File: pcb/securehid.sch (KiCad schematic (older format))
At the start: 93 parts

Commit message: Initial PCB draft
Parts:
- removed C?: 100n, symbol device:C_Small
- removed D? (x4): Ice blue, symbol device:LED
- removed D?: ice blue, symbol device:LED
- removed D? (x5): pink, symbol device:LED
- added C13, C16, C19, C22: 12p, Capacitor_SMD:C_0603_1608Metric_Pad1.05x0.95mm_HandSolder, symbol device:C_Small
- added C30, C31, C35, C36: 100n, Capacitor_SMD:C_0603_1608Metric_Pad1.05x0.95mm_HandSolder, symbol device:C_Small
- added C32, C33: 100n, Capacitor_SMD:C_0603_1608Metric_Pad1.05x0.95mm_HandSolder, symbol device:C
- added C34: 47u, Capacitor_SMD:C_Elec_6.3x5.8, symbol device:CP
- added D11, D12, D13, D14, D15: pink, LED_SMD:LED_PLCC_2835_Handsoldering, symbol device:LED
- added D5, D6, D7, D8, D9: Ice blue, LED_SMD:LED_PLCC_2835_Handsoldering, symbol device:LED
- added J4: SWD_DEVICE, Connector_PinHeader_2.54mm:PinHeader_1x04_P2.54mm_Vertical, symbol Connector_Generic:Conn_01x04
- added R2, R3: 10k, Resistor_SMD:R_0603_1608Metric_Pad1.05x0.95mm_HandSolder, symbol device:R_Small
- added R26: NETTIE, NetTie:NetTie-2_SMD_Pad2.0mm, symbol device:R_Small
- added R4: 1M, Resistor_SMD:R_0603_1608Metric_Pad1.05x0.95mm_HandSolder, symbol device:R_Small
- added TP1, TP10, TP11, TP12, TP13, TP14, TP15, TP16, TP17, TP18, TP19, TP2, TP20, TP21, TP22, TP23, TP24, TP25, TP26, TP27, TP28, TP29, TP3, TP30, TP31, TP32, TP33, TP34, TP35, TP36, TP37, TP38, TP39, TP4, TP40, TP41, TP42, TP43, TP44, TP45, TP46, TP47, TP48, TP49, TP5, TP50, TP51, TP52, TP53, TP54, TP55, TP56, TP57, TP58, TP59, TP6, TP60, TP61, TP62, TP63, TP64, TP65, TP66, TP67, TP68, TP69, TP7, TP70, TP71, TP72, TP73, TP74, TP75, TP76, TP77, TP78, TP79, TP8, TP80, TP9: TestPoint_Alt, TestPoint:TestPoint_Pad_1.0x1.0mm, symbol Connector:TestPoint_Alt
- added U5: AP1117-33, TO_SOT_Packages_SMD:SOT-223-3Lead_TabPin2, symbol regul:AP1117-33
- added Y1: 8MHz, Crystal:Crystal_SMD_TXC_7M-4Pin_3.2x2.5mm, symbol device:Crystal_GND24_Small
- added Y3: 32.768kHz, Crystal:Crystal_SMD_TXC_7M-4Pin_3.2x2.5mm, symbol device:Crystal_GND24_Small
- BT1: renamed from BT?; footprint (none) -> Battery:BatteryHolder_MPD_BC2003_1x2032
- C1, C10, C11, C14, C15, C17, C18, C2, C20, C21, C23, C24, C26, C28, C29, C4, C5, C6, C7, C8: renamed from C?; footprint (none) -> Capacitor_SMD:C_0603_1608Metric_Pad1.05x0.95mm_HandSolder
- C12, C25, C27: renamed from C?; footprint (none) -> Capacitor_SMD:C_Elec_6.3x5.8; ali (none) -> https://www.aliexpress.com/item//32846711940.html
- C9: renamed from C?; footprint (none) -> Capacitor_SMD:C_Elec_10x10.2; ali (none) -> https://www.aliexpress.com/item//32556865449.html
- D1, D16, D17, D18, D19, D2, D20, D21, D22, D23, D24, D3: renamed from D?; footprint (none) -> LED_SMD:LED_0603_1608Metric_Pad1.05x0.95mm_HandSolder
- D10: renamed from D?; footprint (none) -> LED_SMD:LED_PLCC_2835_Handsoldering; ali (none) -> https://www.aliexpress.com/item//32376752790.html
- D4: renamed from D?; footprint (none) -> LED_SMD:LED_PLCC_2835_Handsoldering; ali (none) -> https://www.aliexpress.com/store/product//1758868_326936840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
- J1: renamed from J?; footprint (none) -> Connector_USB:USB_Micro-B_GCT_USB3076-30-A
- J2: renamed from J?; value SWD -> SWD_HOST; footprint (none) -> Connector_PinHeader_2.54mm:PinHeader_1x04_P2.54mm_Vertical
- J3, J5: renamed from J?; footprint (none) -> Connector_PinHeader_2.54mm:PinHeader_1x04_P2.54mm_Vertical
- J6, J8: renamed from J?; footprint (none) -> footprints:USB_A_FEMALE_THT; ali (none) -> https://www.aliexpress.com/item//32849715796.html
- J7: renamed from J?; footprint (none) -> Connector_PinHeader_2.54mm:PinHeader_2x05_P2.54mm_Vertical
- LS1: renamed from LS?; footprint (none) -> Buzzer_Beeper:Buzzer_12x9.5RM7.6; ali (none) -> https://www.aliexpress.com/item//32503620431.html
- R1, R10, R11, R12, R13, R14, R15, R16, R17, R18, R19, R20, R21, R22, R23, R24, R25, R5, R6, R7, R8, R9: renamed from R?; footprint (none) -> Resistor_SMD:R_0603_1608Metric_Pad1.05x0.95mm_HandSolder
- RN1, RN2, RN3: renamed from RN?; footprint (none) -> Resistor_SMD:R_Array_Convex_4x0603; marutsu (none) -> https://www.marutsu.co.jp/pc/i/14222/
- SW1: renamed from SW?; footprint (none) -> Button_Switch_SMD:SW_SPST_EVPBF
- U2: renamed from U?; value STM32F103C8Tx -> STM32F103C8T6
- U3: renamed from U?; value STM32F407VETx -> STM32F407VET6
- U4: renamed from U?; footprint (none) -> Package_SO:SSOP-28_3.9x9.9mm_P0.635mm; ali (none) -> https://www.aliexpress.com/item//32787809220.html
- Y2, Y4: renamed from Y?; footprint (none) -> Crystal:Crystal_SMD_TXC_7M-4Pin_3.2x2.5mm
- gave numbers to parts that had none: 4
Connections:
- net +3V3: now also J4.1 (Pin_1), R2.2; no longer R6.1
- net DBGD_RX: now also U2.31 (PA10)
- net DBGD_TX: now also U2.30 (PA9)
- net GND: now also U3.94 (BOOT0), Y4.2, Y4.4, C19.1, C22.1, C30.1, R26.1, Y3.2, Y3.4; no longer J2.3 (Pin_3), J3.2 (Pin_2), J5.2 (Pin_2)
- net HUB_NRST: now also C30.2
- net LED0: now also RN1.8 (R1.2); no longer D1.1 (K)
- net LED1: now also RN1.7 (R2.2); no longer D2.1 (K)
- net LED10: now also RN3.6 (R3.2); no longer D23.1 (K)
- net LED11: now also RN3.5 (R4.2); no longer D24.1 (K)
- net LED2: now also RN1.6 (R3.2); no longer D3.1 (K)
- net LED3: now also RN1.5 (R4.2); no longer D16.1 (K)
- net LED4: now also RN2.8 (R1.2); no longer D17.1 (K)
- net LED5: now also RN2.7 (R2.2); no longer D18.1 (K)
- net LED6: now also RN2.6 (R3.2); no longer D19.1 (K)
- net LED7: now also RN2.5 (R4.2); no longer D20.1 (K)
- net LED8: now also RN3.8 (R1.2); no longer D21.1 (K)
- net LED9: now also RN3.7 (R2.2); no longer D22.1 (K)
- net SECURE_IF_F4RX: now also U2.12 (PA2)
- net SECURE_IF_F4TX: now also U2.13 (PA3)
- net USBD_DM: now also U2.32 (PA11)
- net USBD_DP: now also U2.33 (PA12)
- net VBUS: now also D1.2 (A), D10.2 (A), D16.2 (A), D17.2 (A), D18.2 (A), D19.2 (A), D2.2 (A), D20.2 (A), D21.2 (A), D22.2 (A), D23.2 (A), D24.2 (A), D3.2 (A), D4.2 (A), C32.1, D11.2 (A), D12.2 (A), D13.2 (A), D14.2 (A), D15.2 (A), D5.2 (A), D6.2 (A), D7.2 (A), D8.2 (A), D9.2 (A), U5.3 (VI); no longer R12.1, R13.1, R14.1, R15.1, R16.1, R17.1, R18.1, R19.1, R20.1, R21.1, R22.1, R23.1, RN1.1 (R1.1), RN1.2 (R2.1), RN1.3 (R3.1), RN1.4 (R4.1), RN2.1 (R1.1), RN2.2 (R2.1), RN2.3 (R3.1), RN2.4 (R4.1), RN3.1 (R1.1), RN3.2 (R2.1), RN3.3 (R3.1), RN3.4 (R4.1)
- net at U3.1 (PE2): now also TP27.1
- net at U3.14 (NRST): now also R2.1
- net at U3.15 (PC0): now also TP52.1
- net at U3.16 (PC1): now also TP54.1
- net at U3.17 (PC2): now also TP56.1
- net at U3.18 (PC3): now also TP58.1
- net at U3.23 (PA0): now also TP1.1
- net at U3.24 (PA1): now also TP2.1
- net at U3.29 (PA4): now also TP3.1
- net at U3.33 (PC4): now also TP60.1
- net at U3.34 (PC5): now also TP62.1
- net at U3.35 (PB0): now also TP20.1
- net at U3.36 (PB1): now also TP24.1
- net at U3.37 (PB2): now also TP28.1
- net at U3.48 (PB11): now also TP46.1
- net at U3.51 (PB12): now also TP47.1
- net at U3.52 (PB13): now also TP48.1
- net at U3.53 (PB14): now also TP49.1
- net at U3.54 (PB15): now also TP50.1
- net at U3.55 (PD8): now also TP67.1
- net at U3.56 (PD9): now also TP69.1
- net at U3.57 (PD10): now also TP71.1
- net at U3.58 (PD11): now also TP73.1
- net at U3.59 (PD12): now also TP75.1
- net at U3.60 (PD13): now also TP77.1
- net at U3.61 (PD14): now also TP79.1
- net at U3.62 (PD15): now also TP80.1
- net at U3.63 (PC6): now also TP64.1
- net at U3.64 (PC7): now also TP66.1
- net at U3.65 (PC8): now also TP68.1
- net at U3.66 (PC9): now also TP70.1
- net at U3.67 (PA8): now also TP5.1
- net at U3.7 (PC13): now also TP78.1
- net at U3.77 (PA15): now also TP14.1
- net at U3.78 (PC10): now also TP72.1
- net at U3.79 (PC11): now also TP74.1
- net at U3.8 (PC14): now also C19.2, Y3.1
- net at U3.80 (PC12): now also TP76.1
- net at U3.81 (PD0): now also TP51.1
- net at U3.82 (PD1): now also TP53.1
- net at U3.83 (PD2): now also TP55.1
- net at U3.84 (PD3): now also TP57.1
- net at U3.85 (PD4): now also TP59.1
- net at U3.86 (PD5): now also TP61.1
- net at U3.87 (PD6): now also TP63.1
- net at U3.88 (PD7): now also TP65.1
- net at U3.89 (PB3): now also TP31.1
- net at U3.9 (PC15): now also C22.2, Y3.3
- net at U3.90 (PB4): now also TP33.1
- net at U3.91 (PB5): now also TP35.1
- net at U3.92 (PB6): now also TP37.1
- net at U3.93 (PB7): now also TP39.1
- net at U3.95 (PB8): now also TP41.1
- net at U3.96 (PB9): now also TP43.1
- net at U3.97 (PE0): now also TP19.1
- net at U3.98 (PE1): now also TP23.1
- net +3.3VA: now reaches U2.1 (VBAT)
- net +3.3VA: now also R6.1, U2.24 (VDD), U2.36 (VDD), U2.48 (VDD), U2.9 (VDDA), C31.1, C33.1, C34.1, C35.1, C36.1, R3.1, U5.2 (VO)
- net at U2.10 (PA0): now also TP9.1
- net at U2.11 (PA1): now also TP11.1
- net at U2.14 (PA4): now also TP16.1
- net at U2.15 (PA5): now also TP18.1
- net at U2.16 (PA6): now also TP22.1
- net at U2.17 (PA7): now also TP26.1
- net at U2.18 (PB0): now also TP8.1
- net at U2.19 (PB1): now also TP10.1
- net at U2.2 (PC13): now also TP4.1
- net at U2.20 (PB2): now also TP12.1
- net at U2.21 (PB10): now also TP34.1
- net at U2.22 (PB11): now also TP36.1
- net GNDA: now reaches U2.23 (VSS)
- net GNDA: now also J2.3 (Pin_3), J3.2 (Pin_2), J5.2 (Pin_2), U2.35 (VSS), U2.44 (BOOT0), U2.47 (VSS), U2.8 (VSSA), C13.1, C16.1, C31.2, C32.2, C33.2, C34.2, C35.2, C36.2, J4.3 (Pin_3), R26.2, U5.1 (GND), Y1.2, Y1.4
- net at U2.25 (PB12): now also TP38.1
- net at U2.26 (PB13): now also TP40.1
- net at U2.27 (PB14): now also TP42.1
- net at U2.28 (PB15): now also TP44.1
- net at U2.29 (PA8): now also TP30.1
- net at U2.3 (PC14): now also TP6.1
- net SWDIOD: now reaches U2.34 (PA13)
- net SWDIOD: now also J4.4 (Pin_4)
- net SWCLKD: now reaches U2.37 (PA14)
- net SWCLKD: now also J4.2 (Pin_2)
- net at U2.38 (PA15): now also TP45.1
- net at U2.39 (PB3): now also TP13.1
- net at U2.4 (PC15): now also TP7.1
- net at U2.40 (PB4): now also TP15.1
- net at U2.41 (PB5): now also TP17.1
- net at U2.42 (PB6): now also TP21.1
- net at U2.43 (PB7): now also TP25.1
- net at U2.45 (PB8): now also TP29.1
- net at U2.46 (PB9): now also TP32.1
- net at U2.5 (PD0): now also C13.2, R4.1, Y1.1
- net at U2.6 (PD1): now also C16.2, R4.2, Y1.3
- net at U2.7 (NRST): now also R3.2
- net at Q1.2 (S): now also R12.2, R13.2, R14.2, R15.2, R16.2, R17.2; no longer D4.1 (K)
- net at Q2.2 (S): now also R18.2, R19.2, R20.2, R21.2, R22.2, R23.2; no longer D10.1 (K)
- net SWCLK renamed SWCLKH
- net SWDIO renamed SWDIOH
- new net: D4.1 (K), R12.1
- new net: D5.1 (K), R13.1
- new net: D6.1 (K), R14.1
- new net: D7.1 (K), R15.1
- new net: D8.1 (K), R16.1
- new net: D9.1 (K), R17.1
- new net: D10.1 (K), R18.1
- new net: D11.1 (K), R19.1
- new net: D12.1 (K), R20.1
- new net: D13.1 (K), R21.1
- new net: D14.1 (K), R22.1
- new net: D15.1 (K), R23.1
- new net: D1.1 (K), RN1.1 (R1.1)
- new net: D2.1 (K), RN1.2 (R2.1)
- new net: D3.1 (K), RN1.3 (R3.1)
- new net: D16.1 (K), RN1.4 (R4.1)
- new net: D17.1 (K), RN2.1 (R1.1)
- new net: D18.1 (K), RN2.2 (R2.1)
- new net: D19.1 (K), RN2.3 (R3.1)
- new net: D20.1 (K), RN2.4 (R4.1)
- new net: D21.1 (K), RN3.1 (R1.1)
- new net: D22.1 (K), RN3.2 (R2.1)
- new net: D23.1 (K), RN3.3 (R3.1)
- new net: D24.1 (K), RN3.4 (R4.1)
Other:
- moved on the sheet: C10, C11, C12, C9, D10, D4, J1, J2, J3, J5, R12, R13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

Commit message: Some cleanups
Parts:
- added TP81, TP82, TP?: TestPoint_Alt, TestPoint:TestPoint_Pad_1.0x1.0mm, symbol Connector:TestPoint_Alt
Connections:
- net GNDA: now also TP?.1
- net SECURE_IF_F4RX: now also TP81.1
- net SECURE_IF_F4TX: now also TP82.1
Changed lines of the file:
@@
 Wire Wire Line
 	13450 4250 14150 4250
-Text Label 14150 3550 2    50   ~ 0
+Text Label 15100 3550 2    50   ~ 0
 SECURE_IF_F4RX
-Text Label 14150 3650 2    50   ~ 0
+Text Label 15100 3650 2    50   ~ 0
 SECURE_IF_F4TX
-Wire Wire Line
-	14150 3650 13450 3650
-Wire Wire Line
-	13450 3550 14150 3550
 $Comp
 L device:Crystal_GND24_Small Y3
@@
 Wire Wire Line
 	1950 1250 2750 1250
+$Comp
+L Connector:TestPoint_Alt TP81
+U 1 1 5BFF0539
+P 14400 3500
+F 0 "TP81" V 14400 3800 50  0000 C CNN
+F 1 "TestPoint_Alt" V 14504 3574 50  0001 C CNN
+F 2 "TestPoint:TestPoint_Pad_1.0x1.0mm" H 14600 3500 50  0001 C CNN
+F 3 "~" H 14600 3500 50  0001 C CNN
+	1    14400 3500
+	0    -1   -1   0
+$EndComp
+$Comp
+L Connector:TestPoint_Alt TP82
+U 1 1 5C0015E1
+P 14400 3600
+F 0 "TP82" V 14400 3900 50  0000 C CNN
+F 1 "TestPoint_Alt" V 14504 3674 50  0001 C CNN
+F 2 "TestPoint:TestPoint_Pad_1.0x1.0mm" H 14600 3600 50  0001 C CNN
+F 3 "~" H 14600 3600 50  0001 C CNN
+	1    14400 3600
+	0    -1   -1   0
+$EndComp
+Wire Wire Line
+	13450 3650 14400 3650
+Wire Wire Line
+	13450 3550 14400 3550
+Wire Wire Line
+	14400 3500 14400 3550
+Connection ~ 14400 3550
+Wire Wire Line
+	14400 3550 15100 3550
+Wire Wire Line
+	14400 3600 14400 3650
+Connection ~ 14400 3650
+Wire Wire Line
+	14400 3650 15100 3650
+$Comp
+L Connector:TestPoint_Alt TP?
+U 1 1 5C13B94B
+P 14400 3700
+F 0 "TP?" V 14400 4000 50  0000 C CNN
+F 1 "TestPoint_Alt" V 14504 3774 50  0001 C CNN
+F 2 "TestPoint:TestPoint_Pad_1.0x1.0mm" H 14600 3700 50  0001 C CNN
+F 3 "~" H 14600 3700 50  0001 C CNN
+	1    14400 3700
+	0    -1   -1   0
+$EndComp
+$Comp
+L power:GNDA #PWR?
+U 1 1 5C14109B
+P 14400 3700
+F 0 "#PWR?" H 14400 3450 50  0001 C CNN
+F 1 "GNDA" H 14405 3527 50  0000 C CNN
+F 2 "" H 14400 3700 50  0001 C CNN
+F 3 "" H 14400 3700 50  0001 C CNN
+	1    14400 3700
+	1    0    0    -1
+$EndComp
 $EndSCHEMATC

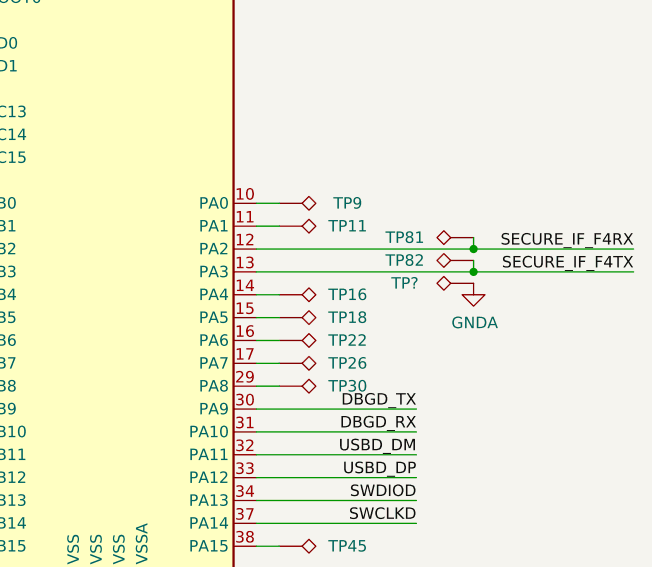
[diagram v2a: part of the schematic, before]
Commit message: Further PCB cleanup, initial silk cleanup
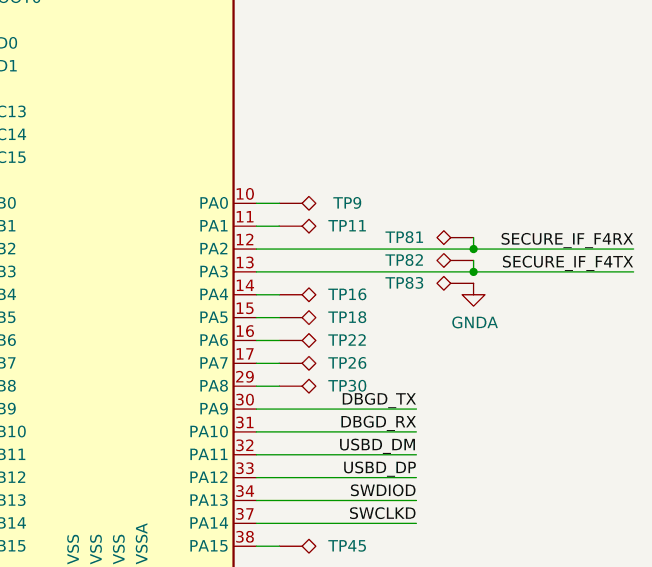
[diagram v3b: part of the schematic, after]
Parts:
- gave numbers to parts that had none: 1
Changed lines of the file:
@@
 	14400 3650 15100 3650
 $Comp
-L Connector:TestPoint_Alt TP?
+L Connector:TestPoint_Alt TP83
 U 1 1 5C13B94B
 P 14400 3700
-F 0 "TP?" V 14400 4000 50  0000 C CNN
+F 0 "TP83" V 14400 4000 50  0000 C CNN
 F 1 "TestPoint_Alt" V 14504 3774 50  0001 C CNN
 F 2 "TestPoint:TestPoint_Pad_1.0x1.0mm" H 14600 3700 50  0001 C CNN
@@
 $EndComp
 $Comp
-L power:GNDA #PWR?
+L power:GNDA #PWR0160
 U 1 1 5C14109B
 P 14400 3700
-F 0 "#PWR?" H 14400 3450 50  0001 C CNN
+F 0 "#PWR0160" H 14400 3450 50  0001 C CNN
 F 1 "GNDA" H 14405 3527 50  0000 C CNN
 F 2 "" H 14400 3700 50  0001 C CNN

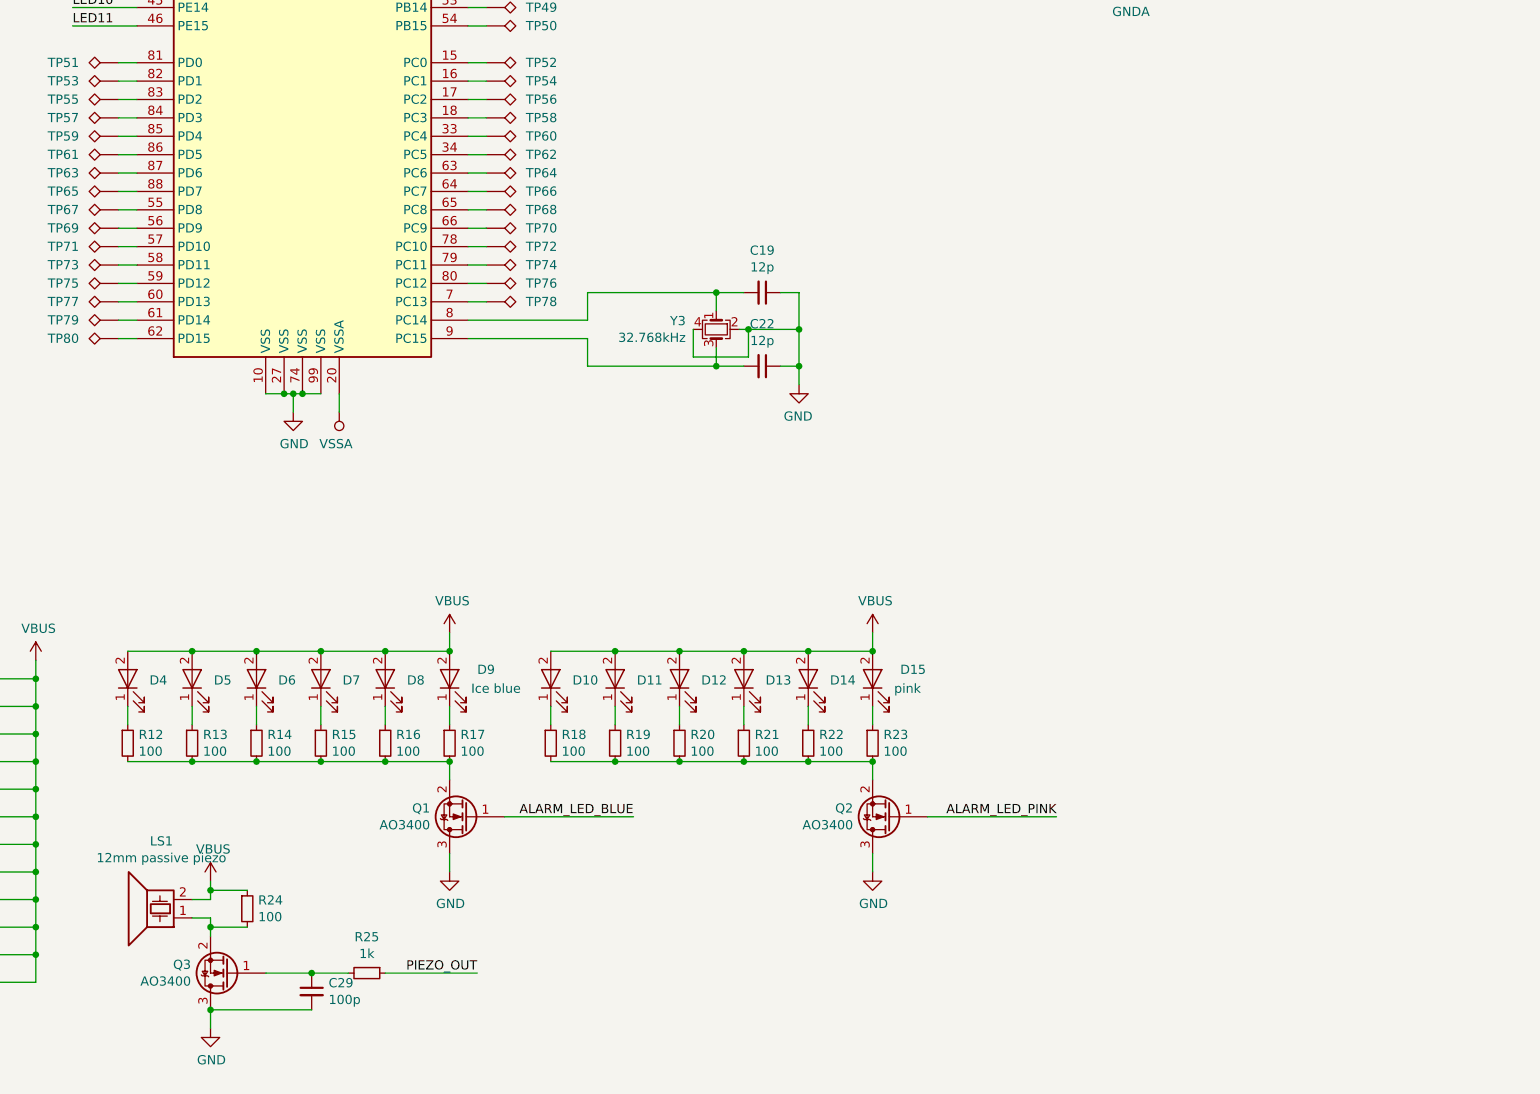
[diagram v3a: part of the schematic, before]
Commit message: pcb: Add BOM
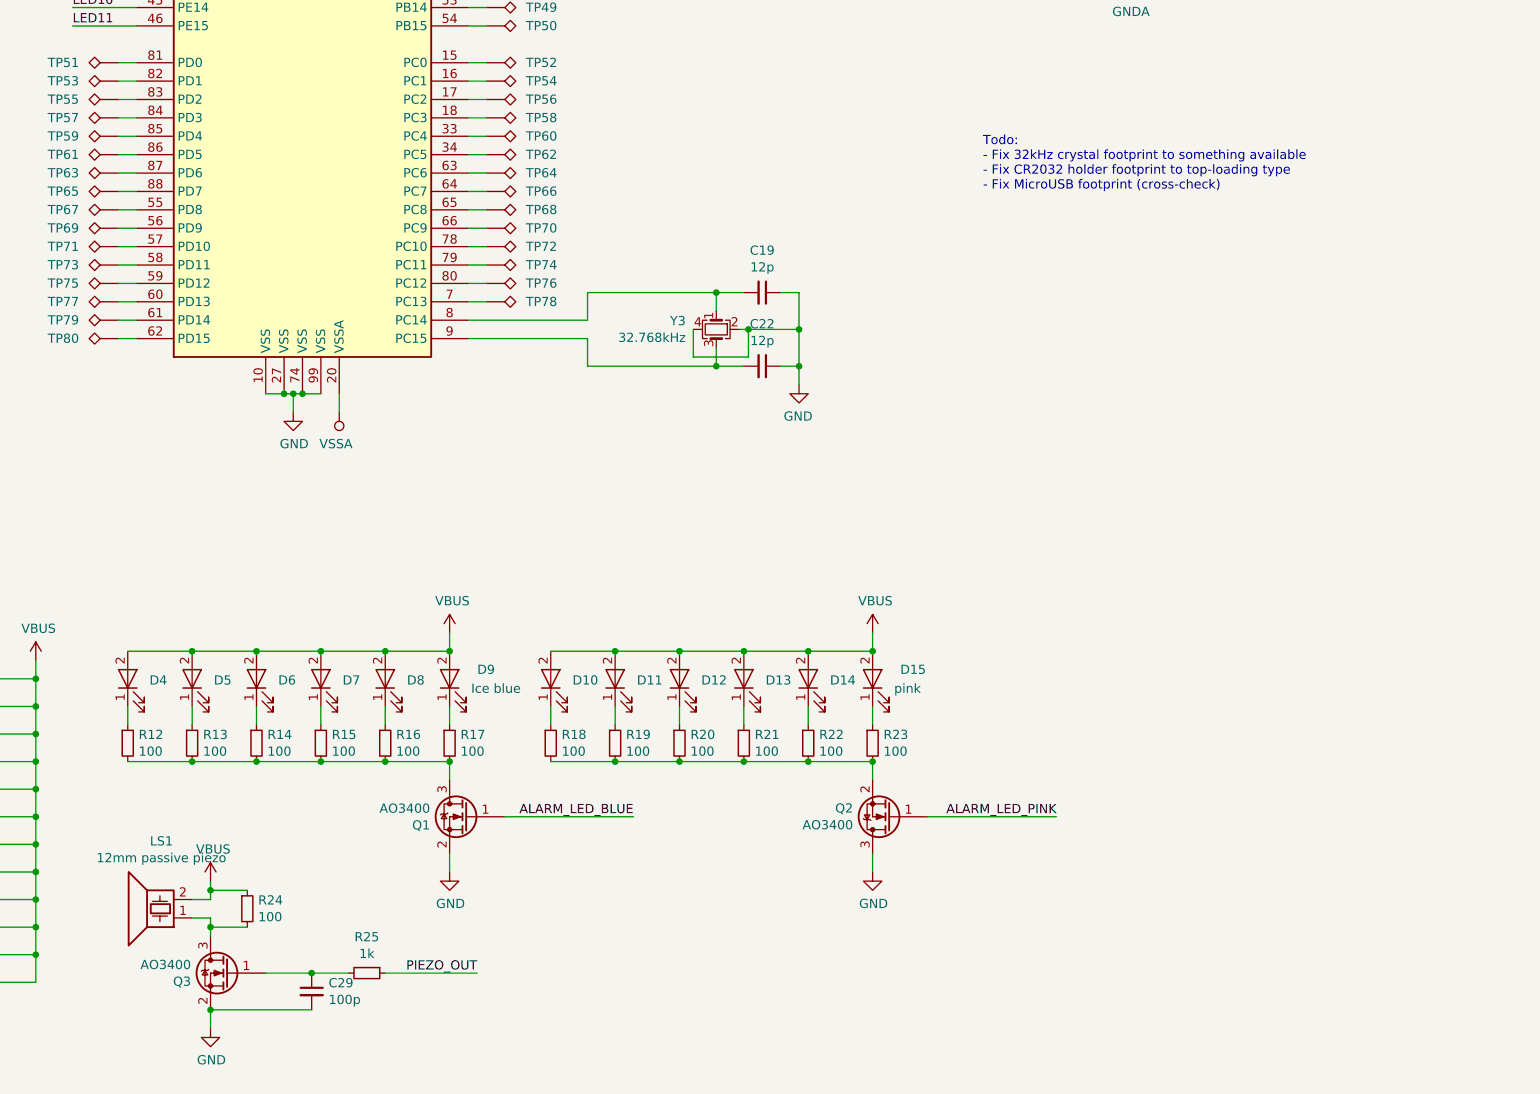
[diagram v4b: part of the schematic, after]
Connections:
- net GND: now also Q1.2 (S), Q3.2 (S); no longer Q1.3 (D), Q3.3 (D)
- net at LS1.1, R24.2: now also Q3.3 (D); no longer Q3.2 (S)
- net at R12.2, R13.2, R14.2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: now also Q1.3 (D); no longer Q1.2 (S)
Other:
- note added: "Todo:\n- Fix 32kHz crystal footprint to something available\n- Fix CR2032 holder footprint to top-loading type\n- Fix MicroUSB footprint (cross-check)"
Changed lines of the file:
@@
 F 3 "https://www.fairchildsemi.com/datasheets/2N/2N7002.pdf" H 9350 9700 50  0001 L CNN
 	1    9350 9700
-	-1   0    0    1
+	-1   0    0    -1
 $EndComp
 $Comp
@@
 F 3 "https://www.fairchildsemi.com/datasheets/2N/2N7002.pdf" H 8050 10550 50  0001 L CNN
 	1    8050 10550
-	-1   0    0    1
+	-1   0    0    -1
 $EndComp
 Wire Wire Line
@@
 Wire Wire Line
 	7950 10750 8500 10750
-Connection ~ 7950 10750
 Wire Wire Line
 	8900 10550 9400 10550
@@
 	1    0    0    -1
 $EndComp
+Text Notes 12150 6300 0    50   ~ 0
+Todo:\n- Fix 32kHz crystal footprint to something available\n- Fix CR2032 holder footprint to top-loading type\n- Fix MicroUSB footprint (cross-check)
+Connection ~ 7950 10750
 $EndSCHEMATC
